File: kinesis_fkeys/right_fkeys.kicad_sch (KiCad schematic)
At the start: 20 parts, among them J1 RIGHT_13_TOP, J3 Conn_01x08

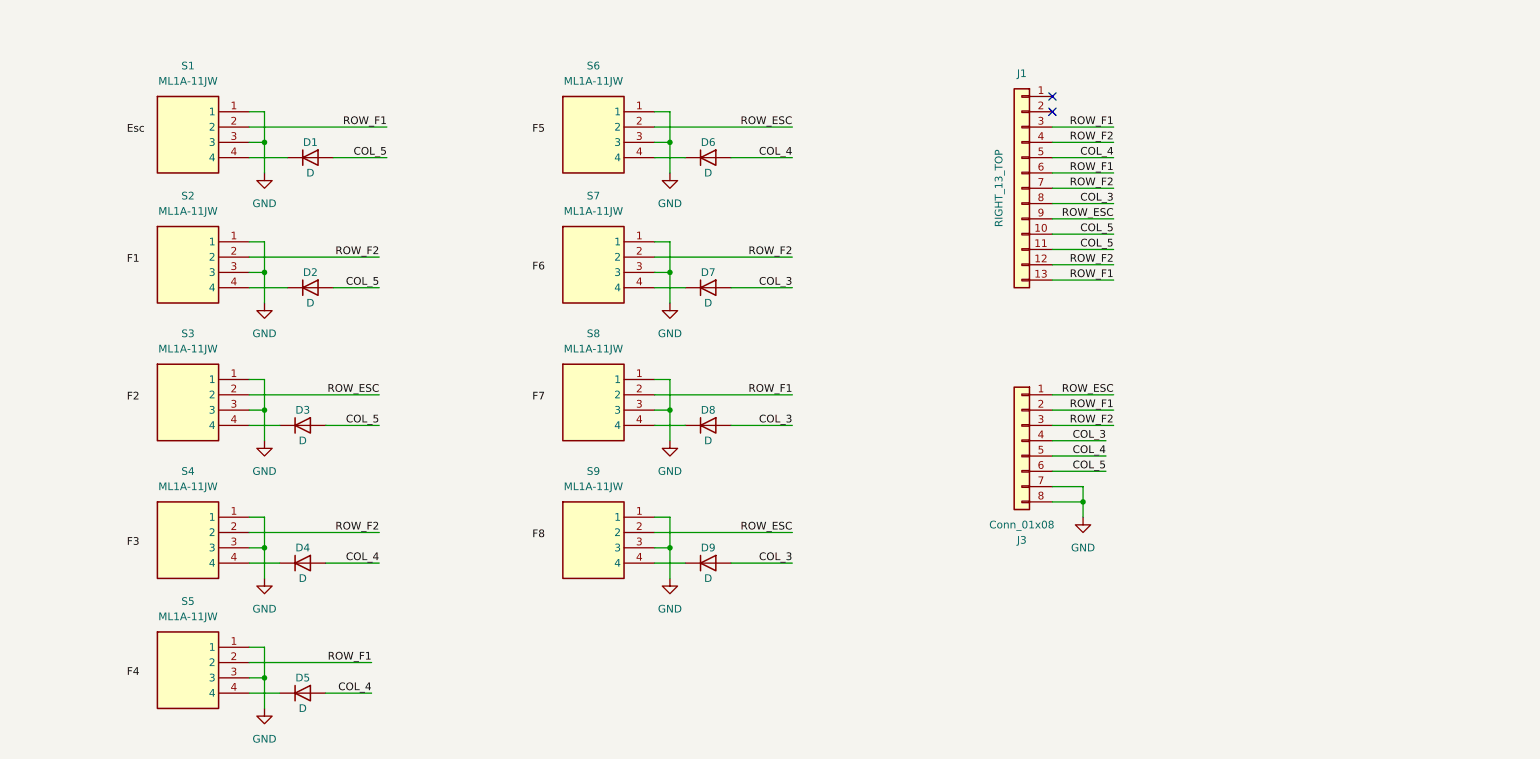
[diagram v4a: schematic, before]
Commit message: positioning of components and added filled zones
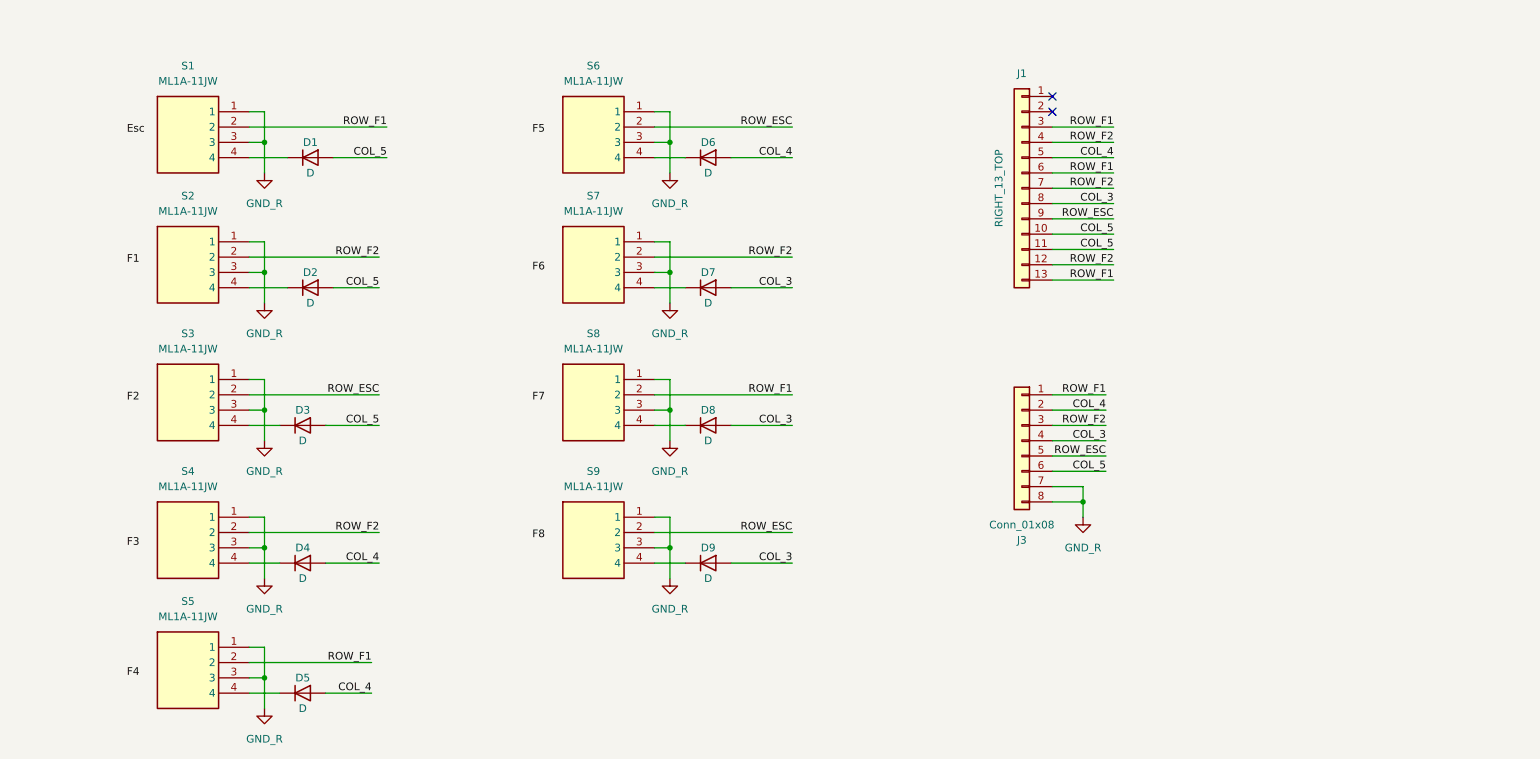
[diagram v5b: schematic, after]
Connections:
- net COL_4: now also J3.2 (Pin_2); no longer J3.5 (Pin_5)
- net ROW_ESC: now also J3.5 (Pin_5); no longer J3.1 (Pin_1)
- net ROW_F1: now also J3.1 (Pin_1); no longer J3.2 (Pin_2)
- net GND renamed GND_R
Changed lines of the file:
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@@
     (stroke (width 0) (type default))
   )
-  (wire (pts (xy 196.85 88.9) (xy 207.01 88.9))
-    (stroke (width 0) (type default))
-  )
-  (wire (pts (xy 196.85 83.82) (xy 207.01 83.82))
+  (wire (pts (xy 196.85 88.9) (xy 205.74 88.9))
+    (stroke (width 0) (type default))
+  )
+  (wire (pts (xy 196.85 83.82) (xy 205.74 83.82))
     (stroke (width 0) (type default))
   )
@@
     (stroke (width 0) (type default))
   )
-  (wire (pts (xy 196.85 86.36) (xy 207.01 86.36))
+  (wire (pts (xy 196.85 86.36) (xy 205.74 86.36))
     (stroke (width 0) (type default))
   )
@@
     (effects (font (size 1.27 1.27)) (justify right bottom))
   )
-  (label "ROW_ESC" (at 207.01 83.82 180) (fields_autoplaced)
+  (label "ROW_ESC" (at 205.74 93.98 180) (fields_autoplaced)
     (effects (font (size 1.27 1.27)) (justify right bottom))
   )
@@
     (effects (font (size 1.27 1.27)) (justify right bottom))
   )
-  (label "COL_4" (at 205.74 93.98 180) (fields_autoplaced)
+  (label "COL_4" (at 205.74 86.36 180) (fields_autoplaced)
     (effects (font (size 1.27 1.27)) (justify right bottom))
   )
@@
     (effects (font (size 1.27 1.27)) (justify right bottom))
   )
-  (label "ROW_F1" (at 207.01 86.36 180) (fields_autoplaced)
+  (label "ROW_F1" (at 205.74 83.82 180) (fields_autoplaced)
     (effects (font (size 1.27 1.27)) (justify right bottom))
   )
@@
     (effects (font (size 1.27 1.27)) (justify right bottom))
   )
-  (label "ROW_F2" (at 207.01 88.9 180) (fields_autoplaced)
+  (label "ROW_F2" (at 205.74 88.9 180) (fields_autoplaced)
     (effects (font (size 1.27 1.27)) (justify right bottom))
   )
@@
       (effects (font (size 1.27 1.27)) hide)
     )
-    (property "Value" "GND" (at 66.04 52.07 0)
+    (property "Value" "GND_R" (at 66.04 52.07 0)
       (effects (font (size 1.27 1.27)))
     )
@@
       (effects (font (size 1.27 1.27)) hide)
     )
-    (property "Value" "GND" (at 66.04 119.38 0)
+    (property "Value" "GND_R" (at 66.04 119.38 0)
       (effects (font (size 1.27 1.27)))
     )
@@
       (effects (font (size 1.27 1.27)) hide)
     )
-    (property "Value" "GND" (at 66.04 96.52 0)
+    (property "Value" "GND_R" (at 66.04 96.52 0)
       (effects (font (size 1.27 1.27)))
     )
@@
       (effects (font (size 1.27 1.27)) hide)
     )
-    (property "Value" "GND" (at 133.35 73.66 0)
+    (property "Value" "GND_R" (at 133.35 73.66 0)
       (effects (font (size 1.27 1.27)))
     )
@@
       (effects (font (size 1.27 1.27)) hide)
     )
-    (property "Value" "GND" (at 133.35 96.52 0)
+    (property "Value" "GND_R" (at 133.35 96.52 0)
       (effects (font (size 1.27 1.27)))
     )
@@
       (effects (font (size 1.27 1.27)) hide)
     )
-    (property "Value" "GND" (at 133.35 119.38 0)
+    (property "Value" "GND_R" (at 133.35 119.38 0)
       (effects (font (size 1.27 1.27)))
     )
@@
       (effects (font (size 1.27 1.27)) hide)
     )
-    (property "Value" "GND" (at 201.93 109.22 0)
+    (property "Value" "GND_R" (at 201.93 109.22 0)
       (effects (font (size 1.27 1.27)))
     )
@@
       (effects (font (size 1.27 1.27)) hide)
     )
-    (property "Value" "GND" (at 133.35 52.07 0)
+    (property "Value" "GND_R" (at 133.35 52.07 0)
       (effects (font (size 1.27 1.27)))
     )
@@
       (effects (font (size 1.27 1.27)) hide)
     )
-    (property "Value" "GND" (at 66.04 73.66 0)
+    (property "Value" "GND_R" (at 66.04 73.66 0)
       (effects (font (size 1.27 1.27)))
     )
@@
       (effects (font (size 1.27 1.27)) hide)
     )
-    (property "Value" "GND" (at 66.04 140.97 0)
-      (effects (font (size 1.27 1.27)))
-    )
+    (property "Value" "GND_R" (at 66.04 140.97 0)
+      (effects (font (size 1.27 1.27)))
+    )

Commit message: created layout - needs to be modified a bit
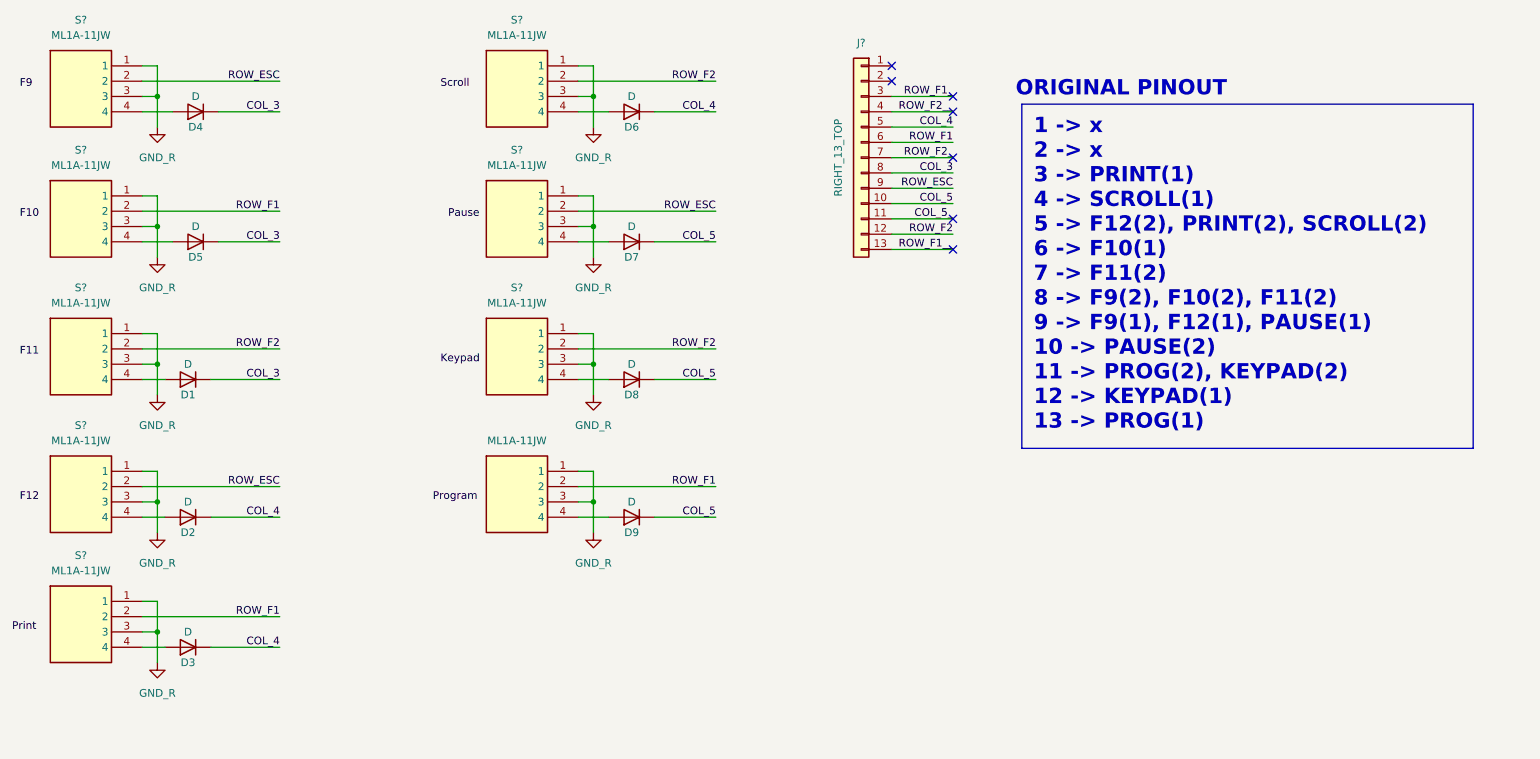
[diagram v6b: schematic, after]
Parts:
- removed J1: RIGHT_13_TOP, dodo_conn:Molex-39-53-2135, symbol Connector_Generic:Conn_01x13
- removed J3: Conn_01x08, dodo_conn:84953-6, symbol Connector_Generic:Conn_01x08
- removed S1, S2, S3, S4, S5, S6, S7, S8, S9: ML1A-11JW, dodo_button_and_switch:ML1A11JW, symbol dodo-buttons:ML1A-11JW
- added J?: RIGHT_13_TOP, dodo_conn:Molex-39-53-2134, symbol Connector_Generic:Conn_01x13
- added S? (x9): ML1A-11JW, dodo_button_and_switch:ML1A11JW, symbol dodo-buttons:ML1A-11JW
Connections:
- net COL_3: now also D1.1 (K), D4.1 (K), D5.1 (K), J?.8 (Pin_8); no longer D7.2 (A), D8.2 (A), D9.2 (A)
- net COL_4: now also D2.1 (K), D3.1 (K), D6.1 (K), J?.5 (Pin_5); no longer D4.2 (A), D5.2 (A), D6.2 (A)
- net COL_5: now also D7.1 (K), D8.1 (K), D9.1 (K), J?.10 (Pin_10); no longer D1.2 (A), D2.2 (A), D3.2 (A)
- net GND_R: now also S?.1, S?.1, S?.1, S?.1, S?.1, S?.1, S?.1, S?.1, S?.1, S?.3, S?.3, S?.3, S?.3, S?.3, S?.3, S?.3, S?.3, S?.3
- net ROW_ESC: now also J?.9 (Pin_9), S?.2, S?.2, S?.2
- net ROW_F1: now also J?.6 (Pin_6), S?.2, S?.2, S?.2
- net ROW_F2: now also J?.12 (Pin_12), S?.2, S?.2, S?.2
- new net: D5.2 (A), S?.4
- new net: D8.2 (A), S?.4
- new net: D1.2 (A), S?.4
- new net: D2.2 (A), S?.4
- new net: D9.2 (A), S?.4
- new net: D7.2 (A), S?.4
- new net: D4.2 (A), S?.4
- new net: D6.2 (A), S?.4
- new net: D3.2 (A), S?.4
- new net COL_5_: J?.11 (Pin_11)
- new net ROW_F1_: J?.3 (Pin_3)
- new net ROW_F1__: J?.13 (Pin_13)
- new net ROW_F2_: J?.7 (Pin_7)
- new net ROW_F2__: J?.4 (Pin_4)
- no-connect marks 2 -> 7
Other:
- note added: "ORIGINAL PINOUT"

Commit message: finished second version of the layout
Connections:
- net COL_5: now also J?.11 (Pin_11); no longer J?.10 (Pin_10)
- net COL_5_: now also J?.10 (Pin_10); no longer J?.11 (Pin_11)
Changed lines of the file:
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@@
   (no_connect (at 170.18 29.21))
   (no_connect (at 180.34 34.29))
-  (no_connect (at 180.34 54.61))
+  (no_connect (at 180.34 52.07))
   (wire (pts (xy 120.65 34.29) (xy 120.65 39.37))
     (stroke (width 0) (type default))
@@
     (effects (font (size 1.27 1.27)) (justify left bottom))
   )
-  (label "COL_5_" (at 180.34 54.61 180) (fields_autoplaced)
+  (label "COL_5_" (at 180.34 52.07 180) (fields_autoplaced)
     (effects (font (size 1.27 1.27)) (justify right bottom))
   )
@@
     (effects (font (size 1.27 1.27)) (justify right bottom))
   )
-  (label "COL_5" (at 180.34 52.07 180) (fields_autoplaced)
-    (effects (font (size 1.27 1.27)) (justify right bottom))
-  )
+  (label "COL_5" (at 180.34 54.61 180) (fields_autoplaced)
+    (effects (font (size 1.27 1.27)) (justify right bottom))
+  )

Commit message: finished layout with successful drc
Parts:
- added JP1, JP2: SolderJumper_2_Open, Jumper:SolderJumper-2_P1.3mm_Open_Pad1.0x1.5mm, symbol Jumper:SolderJumper_2_Open
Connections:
- net ROW_F1: now also JP2.2 (B); no longer S?.2
- net ROW_F2: now also JP1.2 (B); no longer S?.2
- new net: JP2.1 (A), S?.2
- new net: JP1.1 (A), S?.2
